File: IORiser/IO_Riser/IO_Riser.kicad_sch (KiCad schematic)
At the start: 6 parts, among them J1 I/O Port, J2 I/O Port

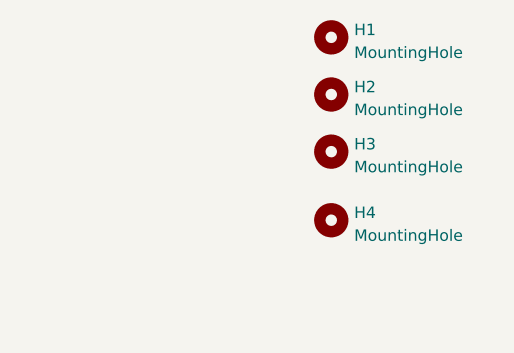
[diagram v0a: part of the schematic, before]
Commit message: rework IO Riser
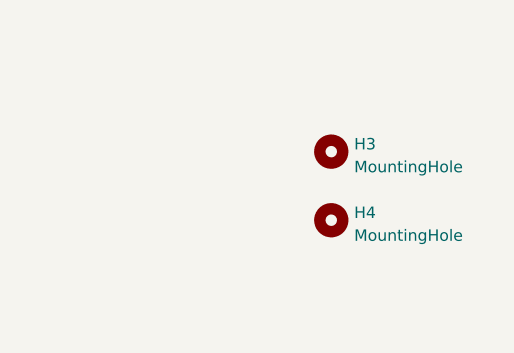
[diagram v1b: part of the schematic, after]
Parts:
- removed H1, H2: MountingHole, MountingHole:MountingHole_3.2mm_M3, symbol Mechanical:MountingHole
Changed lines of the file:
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@@
   (title_block
     (title "TI/99_22 IO RISER")
-    (date "2022-10-16")
-    (rev "V0.5")
+    (date "2022-10-25")
+    (rev "V0.8")
   )
   (junction (at 154.94 78.74) (diameter 0) (color 0 0 0 0)
@@
     )
     (pin "1")
-  )
-  (symbol (lib_id "Mechanical:MountingHole") (at 220.98 38.1 0) (unit 1)
-    (in_bom yes) (on_board yes) (fields_autoplaced)
-    (property "Reference" "H1" (id 0) (at 223.52 37.2653 0)
-      (effects (font (size 1.27 1.27)) (justify left))
-    )
-    (property "Value" "MountingHole" (id 1) (at 223.52 39.8022 0)
-      (effects (font (size 1.27 1.27)) (justify left))
-    )
-    (property "Footprint" "MountingHole:MountingHole_3.2mm_M3" (id 2) (at 220.98 38.1 0)
-      (effects (font (size 1.27 1.27)) hide)
-    )
-    (property "Datasheet" "~" (id 3) (at 220.98 38.1 0)
-      (effects (font (size 1.27 1.27)) hide)
-    )
-  )
-  (symbol (lib_id "Mechanical:MountingHole") (at 220.98 44.45 0) (unit 1)
-    (in_bom yes) (on_board yes) (fields_autoplaced)
-    (property "Reference" "H2" (id 0) (at 223.52 43.6153 0)
-      (effects (font (size 1.27 1.27)) (justify left))
-    )
-    (property "Value" "MountingHole" (id 1) (at 223.52 46.1522 0)
-      (effects (font (size 1.27 1.27)) (justify left))
-    )
-    (property "Footprint" "MountingHole:MountingHole_3.2mm_M3" (id 2) (at 220.98 44.45 0)
-      (effects (font (size 1.27 1.27)) hide)
-    )
-    (property "Datasheet" "~" (id 3) (at 220.98 44.45 0)
-      (effects (font (size 1.27 1.27)) hide)
-    )
   )
   (symbol (lib_id "Mechanical:MountingHole") (at 220.98 50.8 0) (unit 1)
@@
       (reference "#PWR0106") (unit 1) (value "GND") (footprint "")
     )
-    (path "/24681ed6-9547-406f-9e72-569030d43eba"
-      (reference "H1") (unit 1) (value "MountingHole") (footprint "MountingHole:MountingHole_3.2mm_M3")
-    )
-    (path "/32ffb722-4d9e-40d6-b6a9-b8ee8f789477"
-      (reference "H2") (unit 1) (value "MountingHole") (footprint "MountingHole:MountingHole_3.2mm_M3")
-    )
     (path "/35c14355-7297-4f7d-bb96-a3e22ccf81bd"

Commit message: Add BOM
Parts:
- J2: footprint WernerCustomLibrary:Card_edge_44 -> WernerCustomLibrary:44 Pin Card Edge
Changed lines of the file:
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@@
   (title_block
     (title "TI/99_22 IO RISER")
-    (date "2022-10-25")
-    (rev "V0.8")
+    (date "2022-11-19")
+    (rev "V0.9")
   )
   (junction (at 154.94 78.74) (diameter 0) (color 0 0 0 0)
@@
     (property "Reference" "J2" (id 0) (at 160.02 46.99 0))
     (property "Value" "I/O Port" (id 1) (at 160.02 76.2 90))
-    (property "Footprint" "WernerCustomLibrary:Card_edge_44" (id 2) (at 160.02 99.06 0)
+    (property "Footprint" "WernerCustomLibrary:44 Pin Card Edge" (id 2) (at 160.02 99.06 0)
       (effects (font (size 1.524 1.524)) hide)
     )
@@
     )
     (path "/c1730664-01c9-4ced-8530-639cede4365b"
-      (reference "J2") (unit 1) (value "I/O Port") (footprint "WernerCustomLibrary:Card_edge_44")
-    )
-  )
+      (reference "J2") (unit 1) (value "I/O Port") (footprint "WernerCustomLibrary:44 Pin Card Edge")
+    )
+  )
